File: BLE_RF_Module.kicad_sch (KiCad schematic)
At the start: 1 part, among them U2 nRF24L01P

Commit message: First basic design
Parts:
- added AE1: PCB Antenna, RF_Antenna:Texas_SWRA117D_2.4GHz_Right, symbol Device:Antenna_Shield
- added C10: 1p, Capacitor_SMD:C_0402_1005Metric, symbol Device:C_Small
- added C11: 4.7p, Capacitor_SMD:C_0402_1005Metric, symbol Device:C_Small
- added C12: 2.2n, Capacitor_SMD:C_0402_1005Metric, symbol Device:C_Small
- added C3, C4: C_Small, Capacitor_SMD:C_0402_1005Metric, symbol Device:C_Small
- added C5: 33n, Capacitor_SMD:C_0402_1005Metric, symbol Device:C_Small
- added C6: 4.7u, Capacitor_SMD:C_0402_1005Metric, symbol Device:C_Small
- added C7: 10n, Capacitor_SMD:C_0402_1005Metric, symbol Device:C_Small
- added C8: 1n, Capacitor_SMD:C_0402_1005Metric, symbol Device:C_Small
- added C9: 1.5p, Capacitor_SMD:C_0402_1005Metric, symbol Device:C_Small
- added L1: 8.2n, Capacitor_SMD:C_0402_1005Metric, symbol Device:L_Small
- added L2: 2.7n, Capacitor_SMD:C_0402_1005Metric, symbol Device:L_Small
- added L3: 3.9n, Capacitor_SMD:C_0402_1005Metric, symbol Device:L_Small
- added R1: 22k, Capacitor_SMD:C_0402_1005Metric, symbol Device:R_Small
- added Y1: Crystal_GND24_Small, Crystal:Crystal_SMD_3225-4Pin_3.2x2.5mm, symbol Device:Crystal_GND24_Small
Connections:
- net +3V3: now also C6.1, C7.1, C8.1
- net GND: now also AE1.2 (Shield), C10.1, C11.2, C12.2, C3.2, C4.2, C5.2, C6.2, C7.2, C8.2, R1.2, Y1.2, Y1.4
- net XC1: now reaches U2.10 (XC1)
- net XC1: now also C4.1, Y1.3
- net VDD_PA: now reaches U2.11 (VDD_PA)
- net VDD_PA: now also C11.1, C12.1, L2.1
- net ANT1: now reaches U2.12 (ANT1)
- net ANT1: now also L1.2, L2.2
- net ANT2: now reaches U2.13 (ANT2)
- net ANT2: now also L1.1, L3.1
- net at U2.16 (IREF): now also R1.1
- net at U2.19 (DVDD): now also C5.1
- net XC2: now reaches U2.9 (XC2)
- net XC2: now also C3.1, Y1.1
- new net: C9.1, L3.2
- new net: AE1.1 (A), C10.2, C9.2
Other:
- moved on the sheet: U2

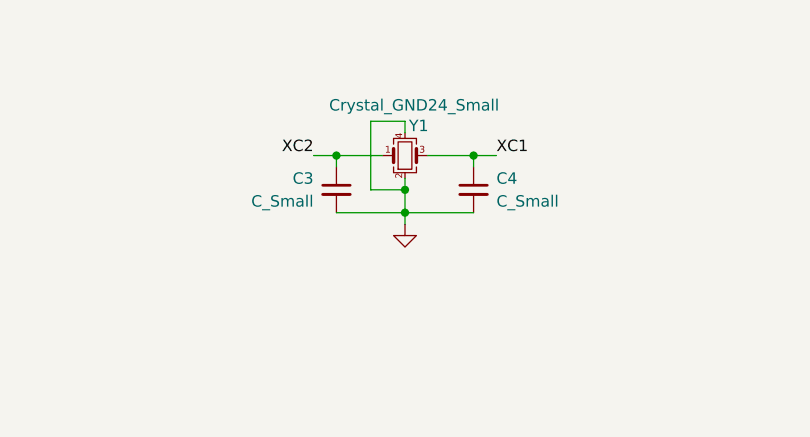
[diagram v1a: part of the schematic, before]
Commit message: BOM assigned
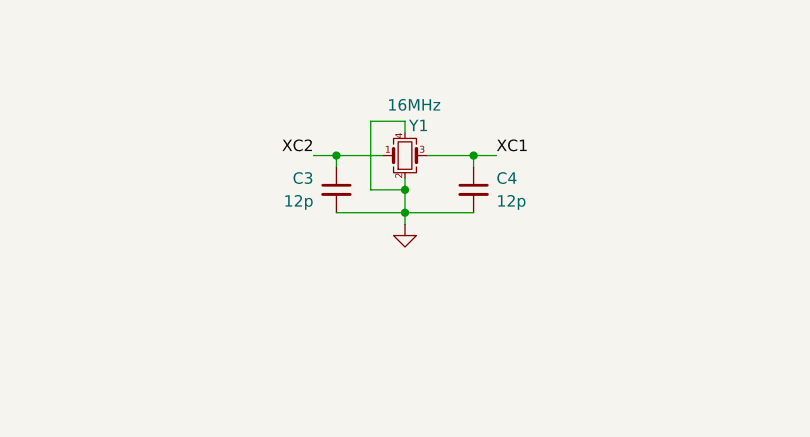
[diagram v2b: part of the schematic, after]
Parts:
- C10: LCSC (none) -> C1550
- C11: LCSC (none) -> C85883
- C12: LCSC (none) -> C126534
- C3, C4: value C_Small -> 12p; LCSC (none) -> C1547
- C5: LCSC (none) -> C301940
- C6: LCSC (none) -> C82453
- C7: LCSC (none) -> C15195
- C8: LCSC (none) -> C1523
- C9: LCSC (none) -> C1552
- L1: LCSC (none) -> C90138
- L2: LCSC (none) -> C370214
- L3: LCSC (none) -> C14033
- R1: LCSC (none) -> C25768
- U2: LCSC (none) -> C8791
- Y1: value Crystal_GND24_Small -> 16MHz; LCSC (none) -> C13738
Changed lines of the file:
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@@
+			)
+		)
+		(property "LCSC" "C90138"
+			(at 67.31 78.74 0)
+			(effects
+				(font
+					(size 1.27 1.27)
+				)
+				(hide yes)
 			)
 		)
@@
 			)
 		)
+		(property "LCSC" "C85883"
+			(at 83.82 96.52 0)
+			(effects
+				(font
+					(size 1.27 1.27)
+				)
+				(hide yes)
+			)
+		)
 		(pin "1"
 		)
@@
 			)
 		)
+		(property "LCSC" "C25768"
+			(at 184.15 95.25 0)
+			(effects
+				(font
+					(size 1.27 1.27)
+				)
+				(hide yes)
+			)
+		)
 		(pin "2"
 		)
@@
 			)
 		)
+		(property "LCSC" "C126534"
+			(at 76.2 96.52 0)
+			(effects
+				(font
+					(size 1.27 1.27)
+				)
+				(hide yes)
+			)
+		)
 		(pin "1"
 		)
@@
 			)
 		)
+		(property "LCSC" "C1523"
+			(at 219.71 29.21 0)
+			(effects
+				(font
+					(size 1.27 1.27)
+				)
+				(hide yes)
+			)
+		)
 		(pin "2"
 		)
@@
 			)
 		)
+		(property "LCSC" "C82453"
+			(at 196.85 29.21 0)
+			(effects
+				(font
+					(size 1.27 1.27)
+				)
+				(hide yes)
+			)
+		)
 		(pin "2"
 		)
@@
 			)
 		)
+		(property "LCSC" "C1552"
+			(at 86.36 73.66 90)
+			(effects
+				(font
+					(size 1.27 1.27)
+				)
+				(hide yes)
+			)
+		)
 		(pin "2"
 		)
@@
 			)
 		)
-		(property "Value" "C_Small"
+		(property "Value" "12p"
 			(at 113.03 38.1062 0)
 			(effects
@@
 		)
 		(property "Description" "Unpolarized capacitor, small symbol"
+			(at 115.57 36.83 0)
+			(effects
+				(font
+					(size 1.27 1.27)
+				)
+				(hide yes)
+			)
+		)
+		(property "LCSC" "C1547"
 			(at 115.57 36.83 0)
 			(effects
@@
 			)
 		)
+		(property "LCSC" "C8791"
+			(at 213.36 77.47 0)
+			(effects
+				(font
+					(size 1.27 1.27)
+				)
+				(hide yes)
+			)
+		)
 		(pin "5"
 		)
@@
 			)
 		)
+		(property "LCSC" "C15195"
+			(at 208.28 29.21 0)
+			(effects
+				(font
+					(size 1.27 1.27)
+				)
+				(hide yes)
+			)
+		)
 		(pin "2"
 		)
@@
 		)
 		(property "Description" "Unpolarized capacitor, small symbol"
+			(at 195.58 95.25 0)
+			(effects
+				(font
+					(size 1.27 1.27)
+				)
+				(hide yes)
+			)
+		)
+		(property "LCSC" "C301940"
 			(at 195.58 95.25 0)
 			(effects
@@
 			)
 		)
+		(property "LCSC" "C14033"
+			(at 74.93 73.66 90)
+			(effects
+				(font
+					(size 1.27 1.27)
+				)
+				(hide yes)
+			)
+		)
 		(pin "1"
 		)
@@
 			)
 		)
-		(property "Value" "C_Small"
+		(property "Value" "12p"
 			(at 133.35 38.1062 0)
 			(effects
@@
 		)
 		(property "Description" "Unpolarized capacitor, small symbol"
+			(at 130.81 36.83 0)
+			(effects
+				(font
+					(size 1.27 1.27)
+				)
+				(hide yes)
+			)
+		)
+		(property "LCSC" "C1547"
 			(at 130.81 36.83 0)
 			(effects
@@
 			)
 		)
+		(property "LCSC" "C370214"
+			(at 74.93 83.82 90)
+			(effects
+				(font
+					(size 1.27 1.27)
+				)
+				(hide yes)
+			)
+		)
 		(pin "1"
 		)
@@
 			)
 		)
-		(property "Value" "Crystal_GND24_Small"
+		(property "Value" "16MHz"
 			(at 124.206 27.432 0)
 			(effects
@@
 		)
 		(property "Description" "Four pin crystal, GND on pins 2 and 4, small symbol"
+			(at 123.19 33.02 0)
+			(effects
+				(font
+					(size 1.27 1.27)
+				)
+				(hide yes)
+			)
+		)
+		(property "LCSC" "C13738"
 			(at 123.19 33.02 0)
 			(effects
@@
 			(at 95.25 77.47 0)
 			(effects
+				(font
+					(size 1.27 1.27)
+				)
+				(hide yes)
+			)
+		)
+		(property "LCSC" "C1550"
+			(at 95.25 77.47 0)
+			(effects

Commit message: Minor changes
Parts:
- AE1: now left out of the parts list
- C10: LCSC C1550 -> (none); MPN (none) -> C1550
- C11: LCSC C85883 -> (none); MPN (none) -> C85883
- C12: LCSC C126534 -> (none); MPN (none) -> C126534
- C3, C4: LCSC C1547 -> (none); MPN (none) -> C1547
- C5: LCSC C301940 -> (none); MPN (none) -> C301940
- C6: LCSC C82453 -> (none); MPN (none) -> C82453
- C7: LCSC C15195 -> (none); MPN (none) -> C15195
- C8: LCSC C1523 -> (none); MPN (none) -> C1523
- C9: LCSC C1552 -> (none); MPN (none) -> C1552
- L1: LCSC C90138 -> (none); MPN (none) -> C90138
- L2: LCSC C370214 -> (none); MPN (none) -> C108255
- L3: LCSC C14033 -> (none); MPN (none) -> C14033
- R1: LCSC C25768 -> (none); MPN (none) -> C25768
- U2: JLCPCB Rotation Offset (none) -> -90; LCSC C8791 -> (none); MPN (none) -> C8791
- Y1: LCSC C13738 -> (none); MPN (none) -> C13738
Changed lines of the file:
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@@
 			)
 		)
-		(property "LCSC" "C90138"
+		(property "MPN" "C90138"
 			(at 67.31 78.74 0)
 			(effects
@@
 			)
 		)
-		(property "LCSC" "C85883"
+		(property "MPN" "C85883"
 			(at 83.82 96.52 0)
 			(effects
@@
 			)
 		)
-		(property "LCSC" "C25768"
+		(property "MPN" "C25768"
 			(at 184.15 95.25 0)
 			(effects
@@
 			)
 		)
-		(property "LCSC" "C126534"
+		(property "MPN" "C126534"
 			(at 76.2 96.52 0)
 			(effects
@@
 			)
 		)
-		(property "LCSC" "C1523"
+		(property "MPN" "C1523"
 			(at 219.71 29.21 0)
 			(effects
@@
 			)
 		)
-		(property "LCSC" "C82453"
+		(property "MPN" "C82453"
 			(at 196.85 29.21 0)
 			(effects
@@
 			)
 		)
-		(property "LCSC" "C1552"
+		(property "MPN" "C1552"
 			(at 86.36 73.66 90)
 			(effects
@@
 			)
 		)
-		(property "LCSC" "C1547"
+		(property "MPN" "C1547"
 			(at 115.57 36.83 0)
 			(effects
@@
 			)
 		)
-		(property "LCSC" "C8791"
+		(property "MPN" "C8791"
+			(at 213.36 77.47 0)
+			(effects
+				(font
+					(size 1.27 1.27)
+				)
+				(hide yes)
+			)
+		)
+		(property "JLCPCB Rotation Offset" "-90"
 			(at 213.36 77.47 0)
 			(effects
@@
 			)
 		)
-		(property "LCSC" "C15195"
+		(property "MPN" "C15195"
 			(at 208.28 29.21 0)
 			(effects
@@
 			)
 		)
-		(property "LCSC" "C301940"
+		(property "MPN" "C301940"
 			(at 195.58 95.25 0)
 			(effects
@@
 			)
 		)
-		(property "LCSC" "C14033"
+		(property "MPN" "C14033"
 			(at 74.93 73.66 90)
 			(effects
@@
 			)
 		)
-		(property "LCSC" "C1547"
+		(property "MPN" "C1547"
 			(at 130.81 36.83 0)
 			(effects
@@
 			)
 		)
-		(property "LCSC" "C370214"
+		(property "MPN" "C108255"
 			(at 74.93 83.82 90)
 			(effects
@@
 			)
 		)
-		(property "LCSC" "C13738"
+		(property "MPN" "C13738"
 			(at 123.19 33.02 0)
 			(effects
@@
 			)
 		)
-		(property "LCSC" "C1550"
+		(property "MPN" "C1550"
 			(at 95.25 77.47 0)
 			(effects
@@
 		(unit 1)
 		(exclude_from_sim no)
-		(in_bom yes)
-		(on_board yes)
-		(dnp no)
+		(in_bom no)
+		(on_board yes)
+		(dnp no)

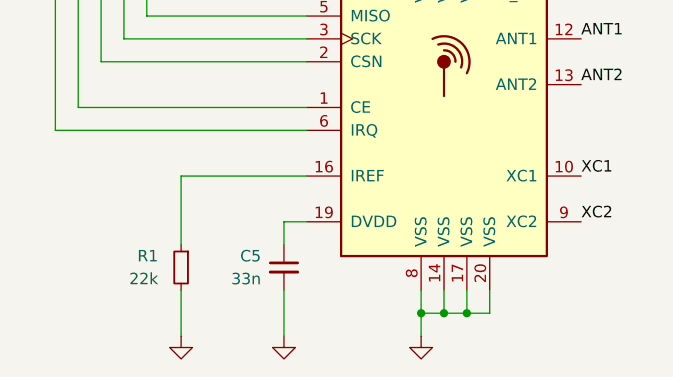
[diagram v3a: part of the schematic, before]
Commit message: Migrated the STM32F0 to an STM32G0B
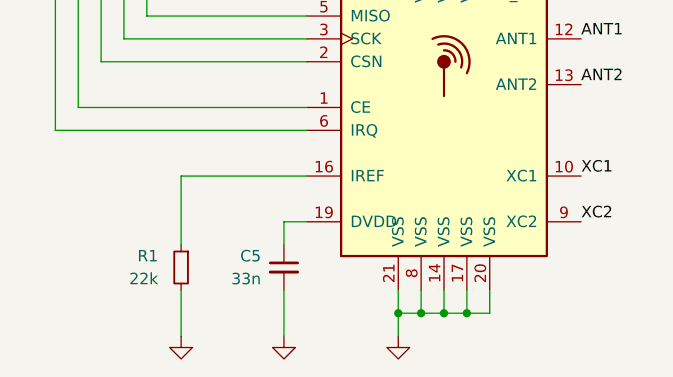
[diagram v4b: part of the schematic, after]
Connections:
- net GND: now also U2.21 (VSS)
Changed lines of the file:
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@@
+	)
+	(junction
+		(at 208.28 100.33)
+		(diameter 0)
+		(color 0 0 0 0)
 	)
 	(junction
@@
 	(wire
 		(pts
+			(xy 208.28 100.33) (xy 210.82 100.33)
+		)
+		(stroke
+			(width 0)
+			(type default)
+		)
+	)
+	(wire
+		(pts
 			(xy 198.12 72.39) (xy 175.26 72.39)
 		)
@@
 	(wire
 		(pts
-			(xy 210.82 100.33) (xy 210.82 102.87)
+			(xy 208.28 100.33) (xy 208.28 102.87)
 		)
 		(stroke
@@
 		(pts
 			(xy 67.31 73.66) (xy 72.39 73.66)
+		)
+		(stroke
+			(width 0)
+			(type default)
+		)
+	)
+	(wire
+		(pts
+			(xy 208.28 97.79) (xy 208.28 100.33)
 		)
 		(stroke
@@
 		(pin "17"
 		)
+		(pin "21"
+		)
 		(instances
 			(project "BLE_board"
@@
 	(symbol
 		(lib_id "power:GND")
-		(at 210.82 102.87 0)
+		(at 208.28 102.87 0)
 		(unit 1)
 		(exclude_from_sim no)
@@
 		(fields_autoplaced yes)
 		(property "Reference" "#PWR04"
-			(at 210.82 109.22 0)
+			(at 208.28 109.22 0)
 			(effects
 				(font
@@
 		)
 		(property "Value" "GND"
-			(at 210.82 107.95 0)
+			(at 208.28 107.95 0)
 			(effects
 				(font
@@
 		)
 		(property "Footprint" ""
-			(at 210.82 102.87 0)
+			(at 208.28 102.87 0)
 			(effects
 				(font
@@
 		)
 		(property "Datasheet" ""
-			(at 210.82 102.87 0)
+			(at 208.28 102.87 0)
 			(effects
 				(font
@@
 		)
 		(property "Description" "Power symbol creates a global label with name \"GND\" , ground"
-			(at 210.82 102.87 0)
-			(effects
-				(font
+			(at 208.28 102.87 0)
+			(effects
+				(font
